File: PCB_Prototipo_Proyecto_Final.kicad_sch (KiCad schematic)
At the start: 1 part, among them J1 VIN

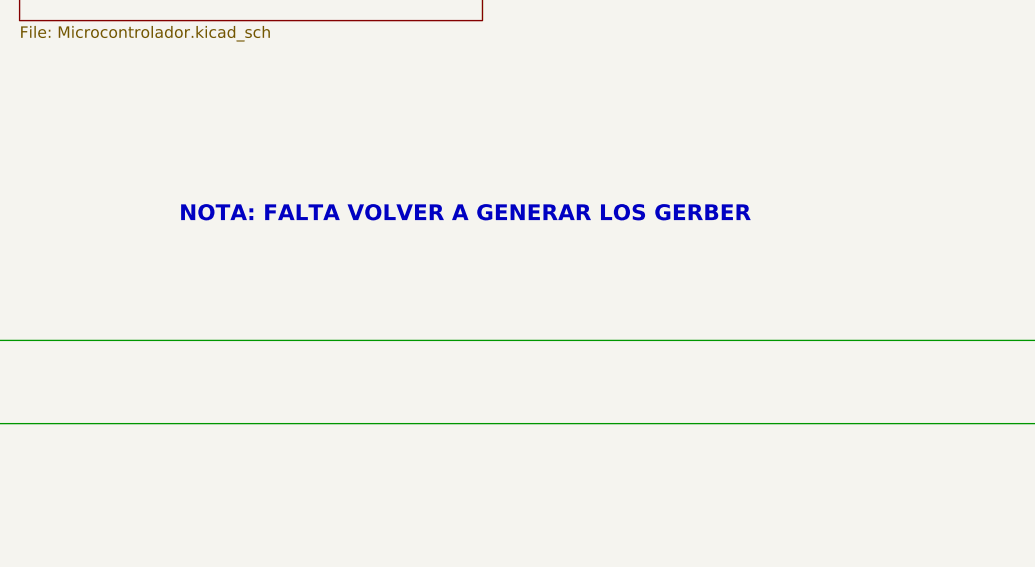
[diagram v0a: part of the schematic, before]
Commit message: Se modificaron algunos componentes, según disponibilidad
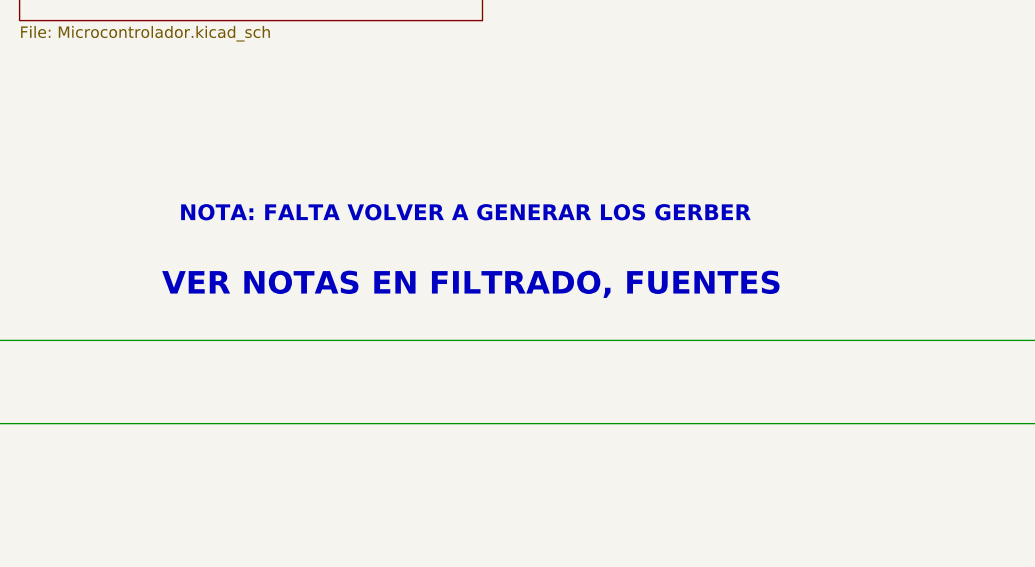
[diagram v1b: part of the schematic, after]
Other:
- note added: "VER NOTAS EN FILTRADO, FUENTES"

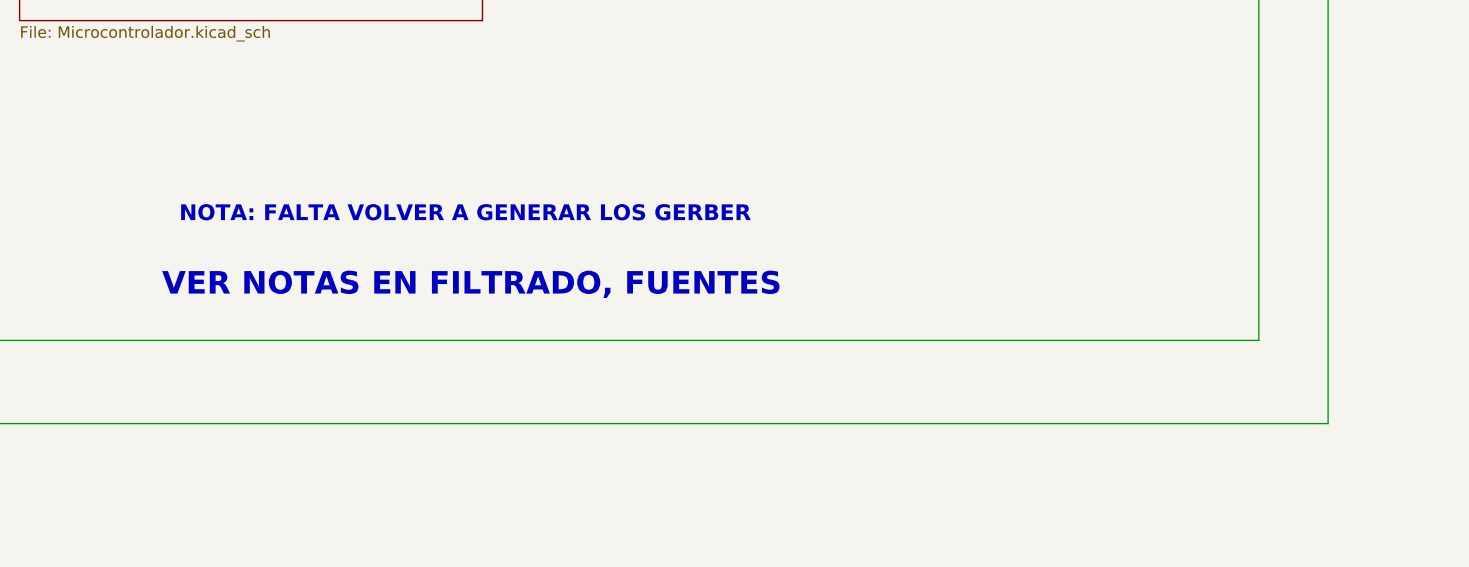
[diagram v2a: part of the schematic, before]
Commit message: Correccion footprints
Se realizo el cambio de algunas footprints segun los componentes disponibles, como los capacitores de 470 uF o la inductancia de la fte switching, y tambien se cambio el LM2596 por el modelo ADJ, con el agregado de un divisor resistivo.
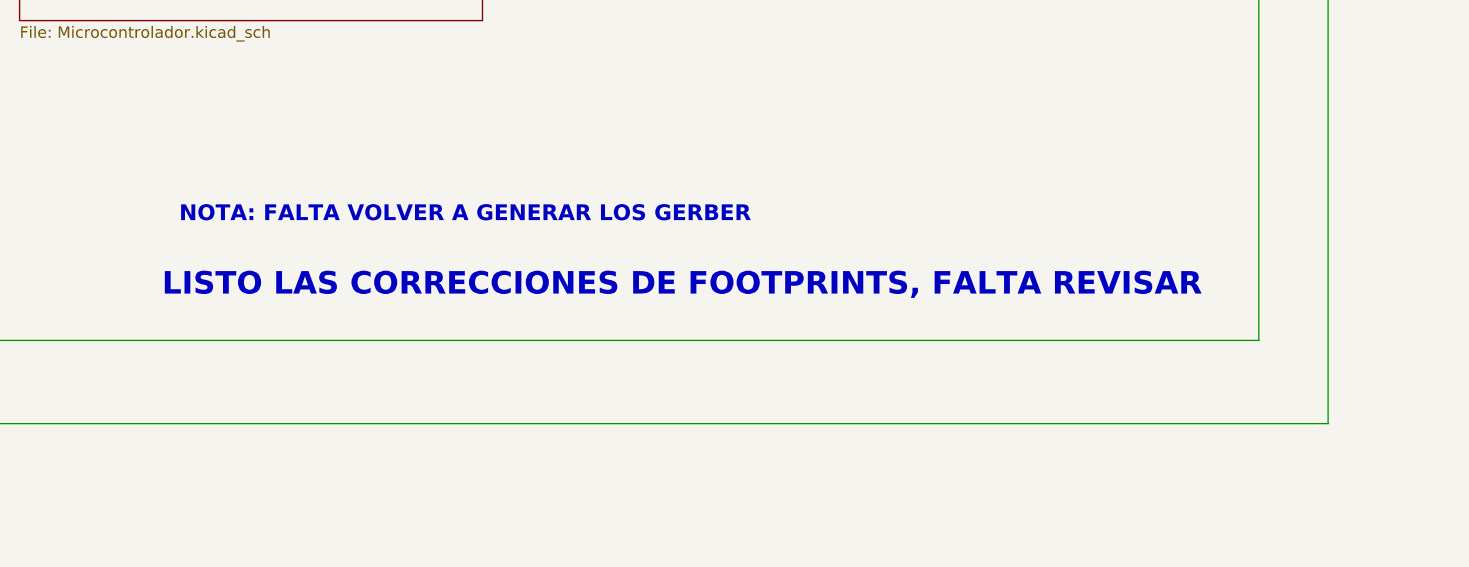
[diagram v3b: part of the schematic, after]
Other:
- note added: "LISTO LAS CORRECCIONES DE FOOTPRINTS, FALTA REVISAR"
- note removed: "VER NOTAS EN FILTRADO, FUENTES"
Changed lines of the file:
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@@
     (stroke (width 0) (type default) (color 0 0 0 0))
   )
-  (text "VER NOTAS EN FILTRADO, FUENTES" (at 138.43 131.445 0)
+  (text "LISTO LAS CORRECCIONES DE FOOTPRINTS, FALTA REVISAR"
+    (at 138.43 131.445 0)
     (effects (font (size 2.5 2.5) (thickness 0.4) bold) (justify left bottom))
   )
@@
       (reference "#PWR011") (unit 1) (value "GND") (footprint "")
     )
+    (path "/5f92bd8c-6854-4ae3-a1d0-b070a0d6afe8/c04aac93-9c28-45f9-bdfe-d3cc9af0b68e"
+      (reference "#PWR012") (unit 1) (value "GND") (footprint "")
+    )
     (path "/aa68080b-efaa-40f4-b3b3-094ea26c340f/d4a29e53-7521-418f-a805-770ff6de9bd3/3c3263dc-93b5-4df0-b6b2-071cab9f1b2c"
       (reference "C1") (unit 1) (value "1 nF") (footprint "Capacitor_SMD:C_0805_2012Metric")
@@
     )
     (path "/5f92bd8c-6854-4ae3-a1d0-b070a0d6afe8/12fc8e7b-24ff-4986-8408-7534acd8b9e1"
-      (reference "C14") (unit 1) (value "470 uF, 50V") (footprint "VE-471M1HTR-1316:CAPAE1300X1650N")
+      (reference "C14") (unit 1) (value "470 uF, 50V") (footprint "Capacitor_THT:CP_Radial_D10.0mm_P5.00mm")
     )
     (path "/5f92bd8c-6854-4ae3-a1d0-b070a0d6afe8/af5e945d-6e41-491f-943f-f54ce556d497"
-      (reference "C15") (unit 1) (value "470 uF, 50V") (footprint "TPSE227K010R0100:TPSE227K016R0100V")
+      (reference "C15") (unit 1) (value "470 uF, 50V") (footprint "Capacitor_THT:CP_Radial_D10.0mm_P5.00mm")
     )
     (path "/5f92bd8c-6854-4ae3-a1d0-b070a0d6afe8/016242b2-7b71-4fed-a00a-3fe8651f8cd2"
@@
     )
     (path "/5f92bd8c-6854-4ae3-a1d0-b070a0d6afe8/90a1e379-e927-402f-93e2-ab05f16b7c25"
-      (reference "C17") (unit 1) (value "10 uF, 50V") (footprint "Capacitor_SMD:C_0805_2012Metric")
+      (reference "C17") (unit 1) (value "10 uF, 50V") (footprint "Capacitor_THT:CP_Radial_D5.0mm_P2.00mm")
     )
     (path "/5f92bd8c-6854-4ae3-a1d0-b070a0d6afe8/80c03b1b-85b6-419f-9d01-74a708f6cf15"
-      (reference "C18") (unit 1) (value "10 uF, 50V") (footprint "Capacitor_SMD:C_0805_2012Metric")
+      (reference "C18") (unit 1) (value "10 uF, 50V") (footprint "Capacitor_THT:CP_Radial_D5.0mm_P2.00mm")
     )
     (path "/922c0b39-92cb-4463-9d8d-3032074eda8e/b47a20aa-eb34-4145-a72d-b3dac59fdda6/864493dd-a5c1-449b-b121-0ae24d08c3eb"
-      (reference "C19") (unit 1) (value "10 uF, 50V") (footprint "Capacitor_SMD:C_0805_2012Metric")
+      (reference "C19") (unit 1) (value "10 uF, 50V") (footprint "Capacitor_THT:CP_Radial_D5.0mm_P2.00mm")
     )
     (path "/922c0b39-92cb-4463-9d8d-3032074eda8e/b47a20aa-eb34-4145-a72d-b3dac59fdda6/2ec62990-1515-41df-808a-208fb752f296"
@@
     )
     (path "/5f92bd8c-6854-4ae3-a1d0-b070a0d6afe8/6a7081b7-501a-4add-a470-2c0d3420af12"
-      (reference "L1") (unit 1) (value "47 uH") (footprint "7447709470:WE-PD_1260_1245_1280_121054")
+      (reference "L1") (unit 1) (value "47 uH") (footprint "Inductor_THT:L_Radial_D7.5mm_P5.00mm_Fastron_07P")
     )
     (path "/922c0b39-92cb-4463-9d8d-3032074eda8e/beef3009-7cac-480a-8e77-cea9adcd939b/681d5973-7300-4dcb-b183-c52c73202d3f"
@@
       (reference "R50") (unit 1) (value "10K, 1/8W") (footprint "Resistor_SMD:R_0805_2012Metric")
     )
-    (path "/5f92bd8c-6854-4ae3-a1d0-b070a0d6afe8/9bc164e6-e873-47da-a2ca-c09dd64582a2"
-      (reference "U1") (unit 1) (value "LM2596S-5") (footprint "Package_TO_SOT_SMD:TO-263-5_TabPin3")
+    (path "/5f92bd8c-6854-4ae3-a1d0-b070a0d6afe8/730b2945-327f-4997-8ae3-e57712129934"
+      (reference "R51") (unit 1) (value "3,3K, 1/8W") (footprint "Resistor_SMD:R_0805_2012Metric")
+    )
+    (path "/5f92bd8c-6854-4ae3-a1d0-b070a0d6afe8/584807d8-8a46-4f4d-8a6b-fa77a640026a"
+      (reference "R52") (unit 1) (value "10K, 1/8W") (footprint "Resistor_SMD:R_0805_2012Metric")
+    )
+    (path "/5f92bd8c-6854-4ae3-a1d0-b070a0d6afe8/d9f3096b-3abf-435d-b796-b01a067f1b95"
+      (reference "U1") (unit 1) (value "LM2596S-ADJ") (footprint "LM2596SX-ADJ_NOPB:LM2596SXADJNOPB")
     )
     (path "/5f92bd8c-6854-4ae3-a1d0-b070a0d6afe8/1d996468-537d-448d-b463-fef17f9a74b3"
-      (reference "U2") (unit 1) (value "LM1117-3.3") (footprint "LM1117SX-3V3-NOPB:KTT0003B")
+      (reference "U2") (unit 1) (value "LM1117-3.3") (footprint "LM1117MPX-33NOPB:SOT230P700X180-4N")
     )
     (path "/922c0b39-92cb-4463-9d8d-3032074eda8e/b47a20aa-eb34-4145-a72d-b3dac59fdda6/a97a44f5-b6f4-4f21-8daf-f76df10ef6c3"

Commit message: Cambios modelos 3D.
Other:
- note removed: "LISTO LAS CORRECCIONES DE FOOTPRINTS, FALTA REVISAR"
- note removed: "NOTA: FALTA VOLVER A GENERAR LOS GERBER"
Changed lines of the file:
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@@
     (stroke (width 0) (type default) (color 0 0 0 0))
   )
-  (text "LISTO LAS CORRECCIONES DE FOOTPRINTS, FALTA REVISAR"
-    (at 138.43 131.445 0)
-    (effects (font (size 2.5 2.5) (thickness 0.4) bold) (justify left bottom))
-  )
   (text "NOTA: DEBIDO A QUE SE BUSCÓ A TODA COSTA QUE\nLA PLACA SEA DE 1 CAPA, SE TUVO QUE UTILIZAR\nEN VARIOS PUNTOS UNA UNION MEDIANTE PIN HEADERS,\nQUE LUEGO SE UNIRAN ENTRE SI MEDIANTE CABLES"
-    (at 191.135 179.07 0)
+    (at 328.93 170.815 0)
     (effects (font (size 1.75 1.75) (thickness 0.254) bold) (justify left bottom))
   )
-  (text "NOTA: FALTA VOLVER A GENERAR LOS GERBER" (at 140.335 123.19 0)
-    (effects (font (size 1.75 1.75) (thickness 0.254) bold) (justify left bottom))
-  )
